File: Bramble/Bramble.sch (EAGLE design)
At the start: 15 parts

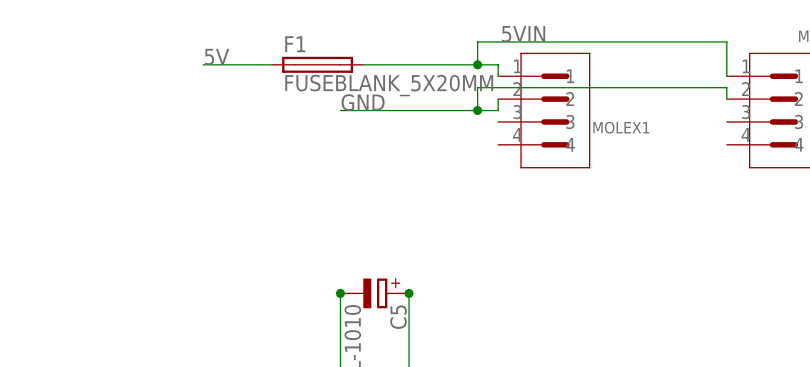
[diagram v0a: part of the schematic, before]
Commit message: Updated fuse holder
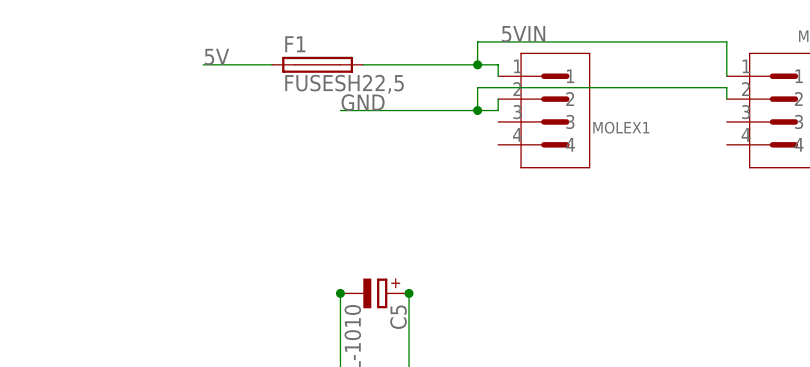
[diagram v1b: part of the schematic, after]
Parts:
- F1: value FUSEBLANK_5X20MM -> FUSESH22,5; device fuse:FUSEBLANK_5X20MM -> fuse:FUSESH22,5
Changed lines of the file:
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@@
 </classes>
 <parts>
-<part name="F1" library="fuse" library_urn="urn:adsk.eagle:library:233" deviceset="FUSE" device="BLANK_5X20MM" package3d_urn="urn:adsk.eagle:package:14079/1"/>
 <part name="JP1" library="Connector" library_urn="urn:adsk.eagle:library:16378166" deviceset="PINHD-2X4" device="/90" package3d_urn="urn:adsk.eagle:package:22465/2"/>
 <part name="C1" library="cap-vishay-153clv" deviceset="CPOL-1010" device=""/>
@@
 <part name="USB12" library="5787745-1" deviceset="5787745-1" device=""/>
 <part name="USB34" library="5787745-1" deviceset="5787745-1" device=""/>
+<part name="F1" library="fuse" library_urn="urn:adsk.eagle:library:233" deviceset="FUSE" device="SH22,5" package3d_urn="urn:adsk.eagle:package:14059/1"/>
 </parts>
 <sheets>
@@
 </plain>
 <instances>
+<instance part="JP1" gate="A" x="93.98" y="20.32" smashed="yes">
+<attribute name="NAME" x="87.63" y="28.575" size="1.778" layer="95"/>
+<attribute name="VALUE" x="87.63" y="12.7" size="1.778" layer="96"/>
+</instance>
+<instance part="C1" gate="G$1" x="7.62" y="68.58" smashed="yes" rot="R180">
+<attribute name="NAME" x="6.477" y="65.5574" size="1.778" layer="95" rot="R180"/>
+<attribute name="VALUE" x="6.477" y="70.6374" size="1.778" layer="96" rot="R180"/>
+</instance>
+<instance part="C2" gate="G$1" x="7.62" y="48.26" smashed="yes" rot="R180">
+<attribute name="NAME" x="6.477" y="45.2374" size="1.778" layer="95" rot="R180"/>
+<attribute name="VALUE" x="6.477" y="50.3174" size="1.778" layer="96" rot="R180"/>
+</instance>
+<instance part="C3" gate="G$1" x="7.62" y="30.48" smashed="yes" rot="R180">
+<attribute name="NAME" x="6.477" y="27.4574" size="1.778" layer="95" rot="R180"/>
+<attribute name="VALUE" x="6.477" y="32.5374" size="1.778" layer="96" rot="R180"/>
+</instance>
+<instance part="C4" gate="G$1" x="7.62" y="7.62" smashed="yes" rot="R180">
+<attribute name="NAME" x="6.477" y="4.5974" size="1.778" layer="95" rot="R180"/>
+<attribute name="VALUE" x="6.477" y="9.6774" size="1.778" layer="96" rot="R180"/>
+</instance>
+<instance part="C5" gate="G$1" x="93.98" y="48.26" smashed="yes" rot="R270">
+<attribute name="NAME" x="97.0026" y="47.117" size="1.778" layer="95" rot="R270"/>
+<attribute name="VALUE" x="91.9226" y="47.117" size="1.778" layer="96" rot="R270"/>
+</instance>
+<instance part="FL1" gate="G$1" x="25.4" y="63.5" smashed="yes">
+<attribute name="NAME" x="12.6956" y="68.58148125" size="2.54148125" layer="95"/>
+<attribute name="VALUE" x="12.69" y="58.413359375" size="2.54331875" layer="96"/>
+</instance>
+<instance part="FL2" gate="G$1" x="25.4" y="43.18" smashed="yes">
+<attribute name="NAME" x="12.6956" y="48.26148125" size="2.54148125" layer="95"/>
+<attribute name="VALUE" x="12.69" y="38.093359375" size="2.54331875" layer="96"/>
+</instance>
+<instance part="FL3" gate="G$1" x="25.4" y="25.4" smashed="yes">
+<attribute name="NAME" x="12.6956" y="30.48148125" size="2.54148125" layer="95"/>
+<attribute name="VALUE" x="12.69" y="20.313359375" size="2.54331875" layer="96"/>
+</instance>
+<instance part="FL4" gate="G$1" x="25.4" y="2.54" smashed="yes">
+<attribute name="NAME" x="12.6956" y="7.62148125" size="2.54148125" layer="95"/>
+<attribute name="VALUE" x="12.69" y="-2.546640625" size="2.54331875" layer="96"/>
+</instance>
+<instance part="MOLEX1" gate="G$1" x="116.84" y="68.58" smashed="yes">
+<attribute name="NAME" x="119.37916875" y="66.041240625" size="1.270209375" layer="95"/>
+</instance>
+<instance part="MOLEX2" gate="G$1" x="142.24" y="68.58" smashed="yes">
+<attribute name="NAME" x="142.23916875" y="76.201240625" size="1.270209375" layer="95"/>
+</instance>
+<instance part="USB12" gate="G$1" x="-20.32" y="55.88" smashed="yes">
+<attribute name="NAME" x="-25.400109375" y="71.7553" size="1.778040625" layer="95"/>
+<attribute name="VALUE" x="-25.40351875" y="38.0877" size="1.77923125" layer="96"/>
+</instance>
+<instance part="USB34" gate="G$1" x="-20.32" y="15.24" smashed="yes">
+<attribute name="NAME" x="-25.400109375" y="31.1153" size="1.778040625" layer="95"/>
+<attribute name="VALUE" x="-25.40351875" y="-2.5523" size="1.77923125" layer="96"/>
+</instance>
 <instance part="F1" gate="G$1" x="88.9" y="73.66" smashed="yes">
 <attribute name="NAME" x="85.09" y="75.057" size="1.778" layer="95"/>
 <attribute name="VALUE" x="85.09" y="70.739" size="1.778" layer="96"/>
-</instance>
-<instance part="JP1" gate="A" x="93.98" y="20.32" smashed="yes">
-<attribute name="NAME" x="87.63" y="28.575" size="1.778" layer="95"/>
-<attribute name="VALUE" x="87.63" y="12.7" size="1.778" layer="96"/>
-</instance>
-<instance part="C1" gate="G$1" x="7.62" y="68.58" smashed="yes" rot="R180">
-<attribute name="NAME" x="6.477" y="65.5574" size="1.778" layer="95" rot="R180"/>
-<attribute name="VALUE" x="6.477" y="70.6374" size="1.778" layer="96" rot="R180"/>
-</instance>
-<instance part="C2" gate="G$1" x="7.62" y="48.26" smashed="yes" rot="R180">
-<attribute name="NAME" x="6.477" y="45.2374" size="1.778" layer="95" rot="R180"/>
-<attribute name="VALUE" x="6.477" y="50.3174" size="1.778" layer="96" rot="R180"/>
-</instance>
-<instance part="C3" gate="G$1" x="7.62" y="30.48" smashed="yes" rot="R180">
-<attribute name="NAME" x="6.477" y="27.4574" size="1.778" layer="95" rot="R180"/>
-<attribute name="VALUE" x="6.477" y="32.5374" size="1.778" layer="96" rot="R180"/>
-</instance>
-<instance part="C4" gate="G$1" x="7.62" y="7.62" smashed="yes" rot="R180">
-<attribute name="NAME" x="6.477" y="4.5974" size="1.778" layer="95" rot="R180"/>
-<attribute name="VALUE" x="6.477" y="9.6774" size="1.778" layer="96" rot="R180"/>
-</instance>
-<instance part="C5" gate="G$1" x="93.98" y="48.26" smashed="yes" rot="R270">
-<attribute name="NAME" x="97.0026" y="47.117" size="1.778" layer="95" rot="R270"/>
-<attribute name="VALUE" x="91.9226" y="47.117" size="1.778" layer="96" rot="R270"/>
-</instance>
-<instance part="FL1" gate="G$1" x="25.4" y="63.5" smashed="yes">
-<attribute name="NAME" x="12.6956" y="68.58148125" size="2.54148125" layer="95"/>
-<attribute name="VALUE" x="12.69" y="58.413359375" size="2.54331875" layer="96"/>
-</instance>
-<instance part="FL2" gate="G$1" x="25.4" y="43.18" smashed="yes">
-<attribute name="NAME" x="12.6956" y="48.26148125" size="2.54148125" layer="95"/>
-<attribute name="VALUE" x="12.69" y="38.093359375" size="2.54331875" layer="96"/>
-</instance>
-<instance part="FL3" gate="G$1" x="25.4" y="25.4" smashed="yes">
-<attribute name="NAME" x="12.6956" y="30.48148125" size="2.54148125" layer="95"/>
-<attribute name="VALUE" x="12.69" y="20.313359375" size="2.54331875" layer="96"/>
-</instance>
-<instance part="FL4" gate="G$1" x="25.4" y="2.54" smashed="yes">
-<attribute name="NAME" x="12.6956" y="7.62148125" size="2.54148125" layer="95"/>
-<attribute name="VALUE" x="12.69" y="-2.546640625" size="2.54331875" layer="96"/>
-</instance>
-<instance part="MOLEX1" gate="G$1" x="116.84" y="68.58" smashed="yes">
-<attribute name="NAME" x="119.37916875" y="66.041240625" size="1.270209375" layer="95"/>
-</instance>
-<instance part="MOLEX2" gate="G$1" x="142.24" y="68.58" smashed="yes">
-<attribute name="NAME" x="142.23916875" y="76.201240625" size="1.270209375" layer="95"/>
-</instance>
-<instance part="USB12" gate="G$1" x="-20.32" y="55.88" smashed="yes">
-<attribute name="NAME" x="-25.400109375" y="71.7553" size="1.778040625" layer="95"/>
-<attribute name="VALUE" x="-25.40351875" y="38.0877" size="1.77923125" layer="96"/>
-</instance>
-<instance part="USB34" gate="G$1" x="-20.32" y="15.24" smashed="yes">
-<attribute name="NAME" x="-25.400109375" y="31.1153" size="1.778040625" layer="95"/>
-<attribute name="VALUE" x="-25.40351875" y="-2.5523" size="1.77923125" layer="96"/>
 </instance>
 </instances>
@@
 <segment>
 <label x="76.2" y="73.66" size="1.778" layer="95"/>
+<wire x1="83.82" y1="73.66" x2="76.2" y2="73.66" width="0.1524" layer="91"/>
 <pinref part="F1" gate="G$1" pin="1"/>
-<wire x1="83.82" y1="73.66" x2="76.2" y2="73.66" width="0.1524" layer="91"/>
 </segment>
 <segment>
@@
 <net name="5VIN" class="0">
 <segment>
-<pinref part="F1" gate="G$1" pin="2"/>
 <wire x1="93.98" y1="73.66" x2="106.68" y2="73.66" width="0.1524" layer="91"/>
 <pinref part="MOLEX1" gate="G$1" pin="1"/>
@@
 <junction x="106.68" y="73.66"/>
 <label x="109.22" y="76.2" size="1.778" layer="95"/>
+<pinref part="F1" gate="G$1" pin="2"/>
 </segment>
 </net>

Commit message: updated board
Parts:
- removed FL1, FL2, FL3, FL4: BLM18KG121TN1D, BLM18PG121SH1D:BLM18PG121SH1D
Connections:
- removed net 5VOUT12: C1.+, C2.+, FL1.1, FL2.1, USB12.VUSB1, USB12.VUSB2
- removed net 5VOUT34: C3.+, C4.+, FL3.1, FL4.1, USB34.VUSB1, USB34.VUSB2
- net 5V: now also C1.+, C2.+, C3.+, C4.+, USB12.VUSB1, USB12.VUSB2, USB34.VUSB1, USB34.VUSB2; no longer FL1.2, FL2.2, FL3.2, FL4.2
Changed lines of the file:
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@@
 <part name="C4" library="cap-vishay-153clv" deviceset="CPOL-1010" device=""/>
 <part name="C5" library="cap-vishay-153clv" deviceset="CPOL-1010" device=""/>
-<part name="FL1" library="BLM18PG121SH1D" deviceset="BLM18PG121SH1D" device="" value="BLM18KG121TN1D"/>
-<part name="FL2" library="BLM18PG121SH1D" deviceset="BLM18PG121SH1D" device="" value="BLM18KG121TN1D"/>
-<part name="FL3" library="BLM18PG121SH1D" deviceset="BLM18PG121SH1D" device="" value="BLM18KG121TN1D"/>
-<part name="FL4" library="BLM18PG121SH1D" deviceset="BLM18PG121SH1D" device="" value="BLM18KG121TN1D"/>
 <part name="MOLEX1" library="15244441" deviceset="15244441" device=""/>
 <part name="MOLEX2" library="15244441" deviceset="15244441" device=""/>
@@
 <attribute name="VALUE" x="91.9226" y="47.117" size="1.778" layer="96" rot="R270"/>
 </instance>
-<instance part="FL1" gate="G$1" x="25.4" y="63.5" smashed="yes">
-<attribute name="NAME" x="12.6956" y="68.58148125" size="2.54148125" layer="95"/>
-<attribute name="VALUE" x="12.69" y="58.413359375" size="2.54331875" layer="96"/>
-</instance>
-<instance part="FL2" gate="G$1" x="25.4" y="43.18" smashed="yes">
-<attribute name="NAME" x="12.6956" y="48.26148125" size="2.54148125" layer="95"/>
-<attribute name="VALUE" x="12.69" y="38.093359375" size="2.54331875" layer="96"/>
-</instance>
-<instance part="FL3" gate="G$1" x="25.4" y="25.4" smashed="yes">
-<attribute name="NAME" x="12.6956" y="30.48148125" size="2.54148125" layer="95"/>
-<attribute name="VALUE" x="12.69" y="20.313359375" size="2.54331875" layer="96"/>
-</instance>
-<instance part="FL4" gate="G$1" x="25.4" y="2.54" smashed="yes">
-<attribute name="NAME" x="12.6956" y="7.62148125" size="2.54148125" layer="95"/>
-<attribute name="VALUE" x="12.69" y="-2.546640625" size="2.54331875" layer="96"/>
-</instance>
 <instance part="MOLEX1" gate="G$1" x="116.84" y="68.58" smashed="yes">
 <attribute name="NAME" x="119.37916875" y="66.041240625" size="1.270209375" layer="95"/>
@@
 <net name="5V" class="0">
 <segment>
-<label x="43.18" y="63.5" size="1.778" layer="95"/>
-<pinref part="FL1" gate="G$1" pin="2"/>
-<wire x1="38.1" y1="63.5" x2="48.4124" y2="63.5" width="0.1524" layer="91"/>
-<junction x="38.1" y="63.5"/>
+<label x="17.78" y="63.5" size="1.778" layer="95"/>
+<wire x1="7.62" y1="63.5" x2="23.0124" y2="63.5" width="0.1524" layer="91"/>
+<wire x1="-7.62" y1="63.5" x2="7.62" y2="63.5" width="0.1524" layer="91"/>
+<pinref part="C1" gate="G$1" pin="+"/>
+<junction x="7.62" y="63.5"/>
+<label x="-7.62" y="63.5" size="1.778" layer="95"/>
 </segment>
 <segment>
@@
 </segment>
 <segment>
-<label x="43.18" y="43.18" size="1.778" layer="95"/>
-<wire x1="38.1" y1="43.18" x2="48.4124" y2="43.18" width="0.1524" layer="91"/>
-<pinref part="FL2" gate="G$1" pin="2"/>
-</segment>
-<segment>
-<label x="43.18" y="25.4" size="1.778" layer="95"/>
-<wire x1="48.26" y1="25.4" x2="38.1" y2="25.4" width="0.1524" layer="91"/>
-<pinref part="FL3" gate="G$1" pin="2"/>
-</segment>
-<segment>
-<label x="43.18" y="2.54" size="1.778" layer="95"/>
-<wire x1="48.26" y1="2.54" x2="38.1" y2="2.54" width="0.1524" layer="91"/>
-<pinref part="FL4" gate="G$1" pin="2"/>
+<label x="17.78" y="43.18" size="1.778" layer="95"/>
+<wire x1="7.62" y1="43.18" x2="23.0124" y2="43.18" width="0.1524" layer="91"/>
+<wire x1="-7.62" y1="43.18" x2="7.62" y2="43.18" width="0.1524" layer="91"/>
+<pinref part="C2" gate="G$1" pin="+"/>
+<junction x="7.62" y="43.18"/>
+<label x="-7.62" y="43.18" size="1.778" layer="95"/>
+</segment>
+<segment>
+<label x="17.78" y="25.4" size="1.778" layer="95"/>
+<wire x1="22.86" y1="25.4" x2="7.62" y2="25.4" width="0.1524" layer="91"/>
+<wire x1="-7.62" y1="25.4" x2="7.62" y2="25.4" width="0.1524" layer="91"/>
+<pinref part="C3" gate="G$1" pin="+"/>
+<junction x="7.62" y="25.4"/>
+<label x="-7.62" y="25.4" size="1.778" layer="95"/>
 </segment>
 <segment>
@@
 <junction x="99.06" y="48.26"/>
 </segment>
+<segment>
+<wire x1="-7.62" y1="2.54" x2="7.62" y2="2.54" width="0.1524" layer="91"/>
+<pinref part="C4" gate="G$1" pin="+"/>
+<junction x="7.62" y="2.54"/>
+<label x="-7.62" y="2.54" size="1.778" layer="95"/>
+<label x="17.78" y="2.54" size="1.778" layer="95"/>
+<wire x1="22.86" y1="2.54" x2="7.62" y2="2.54" width="0.1524" layer="91"/>
+</segment>
+<segment>
+<wire x1="-35.56" y1="68.58" x2="-30.48" y2="68.58" width="0.1524" layer="91"/>
+<pinref part="USB12" gate="G$1" pin="VUSB1"/>
+<label x="-38.1" y="68.58" size="1.778" layer="95"/>
+</segment>
+<segment>
+<wire x1="-35.56" y1="55.88" x2="-30.48" y2="55.88" width="0.1524" layer="91"/>
+<pinref part="USB12" gate="G$1" pin="VUSB2"/>
+<label x="-38.1" y="55.88" size="1.778" layer="95"/>
+</segment>
+<segment>
+<wire x1="-35.56" y1="27.94" x2="-30.48" y2="27.94" width="0.1524" layer="91"/>
+<pinref part="USB34" gate="G$1" pin="VUSB1"/>
+<label x="-38.1" y="27.94" size="1.778" layer="95"/>
+</segment>
+<segment>
+<wire x1="-35.56" y1="15.24" x2="-30.48" y2="15.24" width="0.1524" layer="91"/>
+<pinref part="USB34" gate="G$1" pin="VUSB2"/>
+<label x="-38.1" y="15.24" size="1.778" layer="95"/>
+</segment>
 </net>
 <net name="GND" class="0">
@@
 </segment>
 </net>
-<net name="5VOUT12" class="0">
-<segment>
-<wire x1="-35.56" y1="68.58" x2="-30.48" y2="68.58" width="0.1524" layer="91"/>
-<pinref part="USB12" gate="G$1" pin="VUSB1"/>
-<label x="-38.1" y="68.58" size="1.778" layer="95"/>
-</segment>
-<segment>
-<wire x1="-35.56" y1="55.88" x2="-30.48" y2="55.88" width="0.1524" layer="91"/>
-<pinref part="USB12" gate="G$1" pin="VUSB2"/>
-<label x="-38.1" y="55.88" size="1.778" layer="95"/>
-</segment>
-<segment>
-<wire x1="-7.62" y1="63.5" x2="7.62" y2="63.5" width="0.1524" layer="91"/>
-<pinref part="C1" gate="G$1" pin="+"/>
-<wire x1="7.62" y1="63.5" x2="10.16" y2="63.5" width="0.1524" layer="91"/>
-<junction x="7.62" y="63.5"/>
-<pinref part="FL1" gate="G$1" pin="1"/>
-<label x="-7.62" y="63.5" size="1.778" layer="95"/>
-</segment>
-<segment>
-<wire x1="-7.62" y1="43.18" x2="7.62" y2="43.18" width="0.1524" layer="91"/>
-<pinref part="C2" gate="G$1" pin="+"/>
-<wire x1="7.62" y1="43.18" x2="10.16" y2="43.18" width="0.1524" layer="91"/>
-<junction x="7.62" y="43.18"/>
-<pinref part="FL2" gate="G$1" pin="1"/>
-<label x="-7.62" y="43.18" size="1.778" layer="95"/>
-</segment>
-</net>
-<net name="5VOUT34" class="0">
-<segment>
-<wire x1="-35.56" y1="27.94" x2="-30.48" y2="27.94" width="0.1524" layer="91"/>
-<pinref part="USB34" gate="G$1" pin="VUSB1"/>
-<label x="-38.1" y="27.94" size="1.778" layer="95"/>
-</segment>
-<segment>
-<wire x1="-7.62" y1="25.4" x2="7.62" y2="25.4" width="0.1524" layer="91"/>
-<pinref part="C3" gate="G$1" pin="+"/>
-<wire x1="7.62" y1="25.4" x2="10.16" y2="25.4" width="0.1524" layer="91"/>
-<junction x="7.62" y="25.4"/>
-<pinref part="FL3" gate="G$1" pin="1"/>
-<label x="-7.62" y="25.4" size="1.778" layer="95"/>
-</segment>
-<segment>
-<wire x1="-35.56" y1="15.24" x2="-30.48" y2="15.24" width="0.1524" layer="91"/>
-<pinref part="USB34" gate="G$1" pin="VUSB2"/>
-<label x="-38.1" y="15.24" size="1.778" layer="95"/>
-</segment>
-<segment>
-<wire x1="-7.62" y1="2.54" x2="7.62" y2="2.54" width="0.1524" layer="91"/>
-<pinref part="C4" gate="G$1" pin="+"/>
-<wire x1="7.62" y1="2.54" x2="10.16" y2="2.54" width="0.1524" layer="91"/>
-<junction x="7.62" y="2.54"/>
-<pinref part="FL4" gate="G$1" pin="1"/>
-<label x="-7.62" y="2.54" size="1.778" layer="95"/>
-</segment>
-</net>
